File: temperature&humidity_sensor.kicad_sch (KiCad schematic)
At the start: 4 parts, among them U36 HDC1080

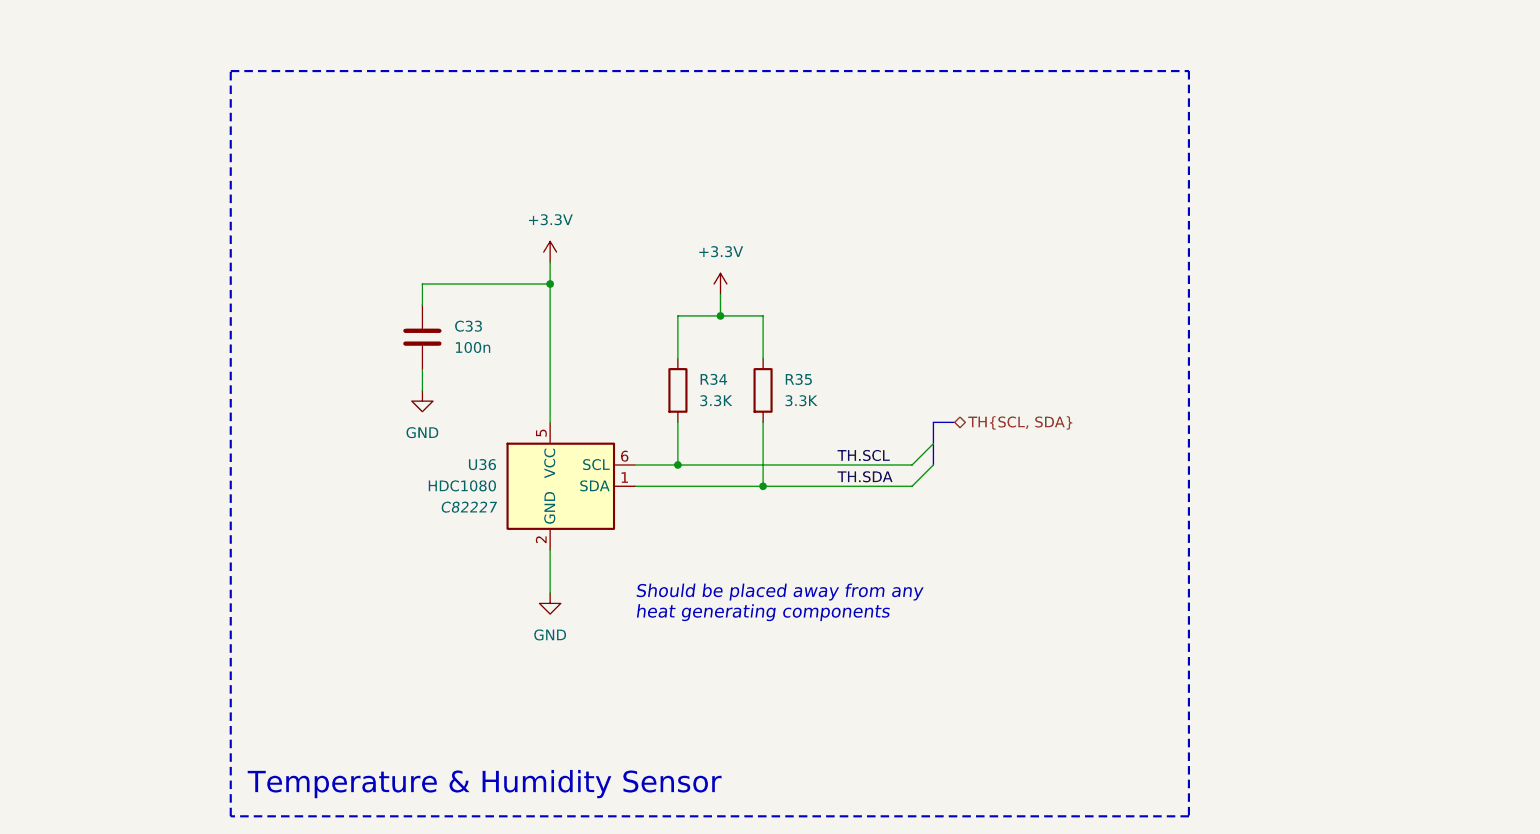
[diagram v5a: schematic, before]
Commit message: ESD, LEDs, footprints
- assignment of footprints
- ESD protection
- User buttons
- addition of test points
- BOM consolidation of  resistors
- general reordering of the schematic
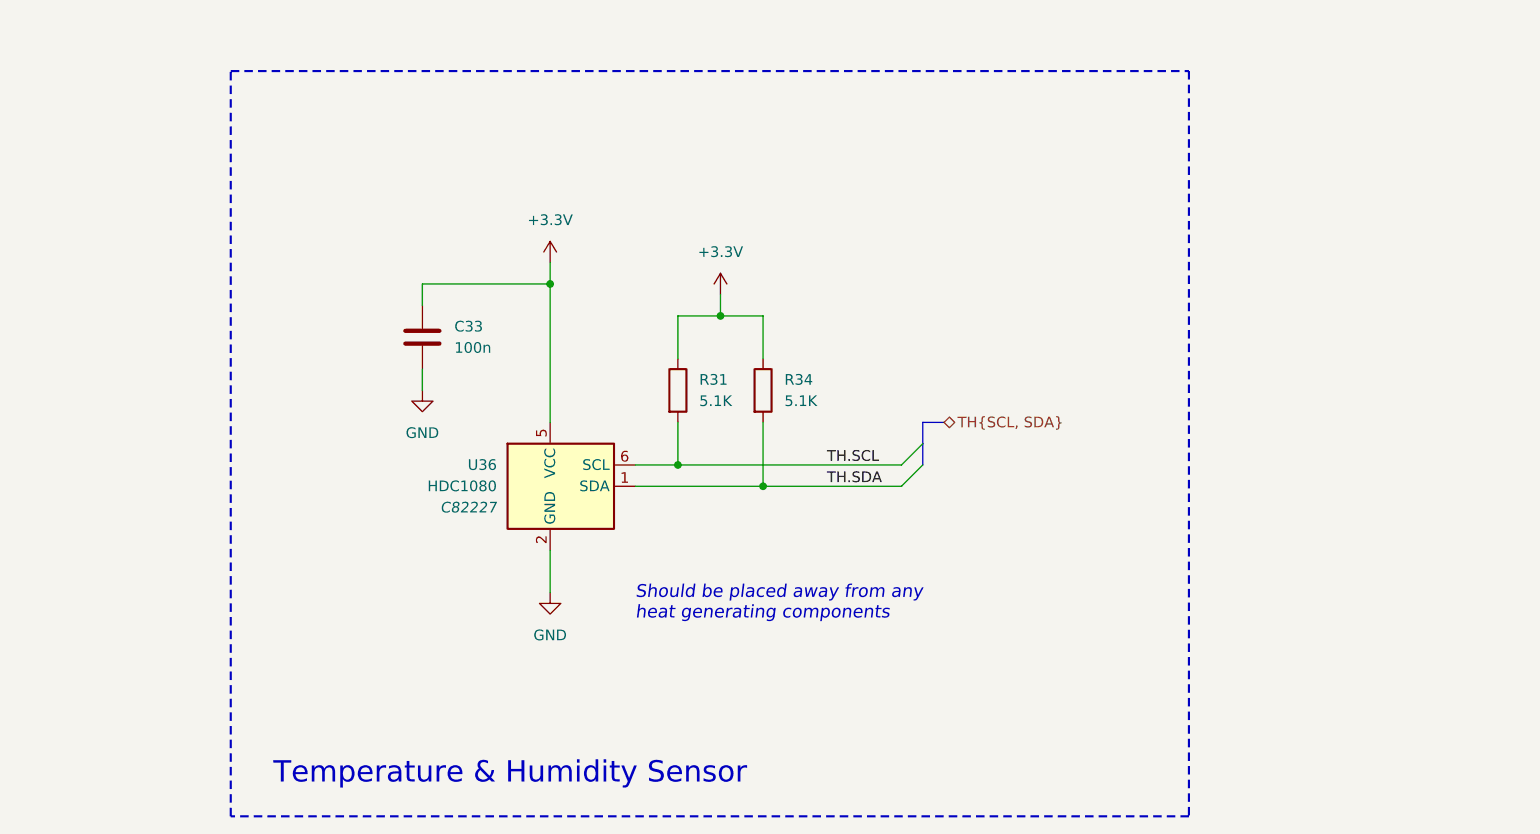
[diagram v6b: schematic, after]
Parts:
- removed R35: 3.3K, symbol Device:R
- added R31: 5.1K, Resistor_SMD:R_0603_1608Metric, symbol Device:R
- C33: footprint (none) -> Capacitor_SMD:C_0603_1608Metric
- R34: value 3.3K -> 5.1K; footprint (none) -> Resistor_SMD:R_0603_1608Metric
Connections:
- net +3.3V: now also R31.1
- net TH.SCL: now also R31.2; no longer R34.2
- net TH.SDA: now also R34.2
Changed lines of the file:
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@@
 	(title_block
 		(title "Temperature & Humidity Sensor")
-		(date "2025-10-31")
+		(date "2025-11-04")
 		(rev "v0.0")
 		(company "Rajath Katker")
@@
 	(text "Temperature & Humidity Sensor"
 		(exclude_from_sim no)
-		(at 84.582 142.24 0)
+		(at 87.63 140.97 0)
 		(effects
 			(font
@@
 	)
 	(bus_entry
-		(at 166.37 101.6)
+		(at 165.1 101.6)
 		(size -2.54 2.54)
 		(stroke
@@
 	)
 	(bus_entry
-		(at 166.37 104.14)
+		(at 165.1 104.14)
 		(size -2.54 2.54)
 		(stroke
@@
 	(wire
 		(pts
-			(xy 146.05 106.68) (xy 163.83 106.68)
+			(xy 146.05 106.68) (xy 162.56 106.68)
 		)
 		(stroke
@@
 	(wire
 		(pts
-			(xy 135.89 104.14) (xy 163.83 104.14)
+			(xy 135.89 104.14) (xy 162.56 104.14)
 		)
 		(stroke
@@
 	(bus
 		(pts
-			(xy 166.37 99.06) (xy 166.37 101.6)
+			(xy 165.1 99.06) (xy 165.1 101.6)
 		)
 		(stroke
@@
 	(bus
 		(pts
-			(xy 166.37 101.6) (xy 166.37 104.14)
+			(xy 165.1 101.6) (xy 165.1 104.14)
 		)
 		(stroke
@@
 	(bus
 		(pts
-			(xy 166.37 99.06) (xy 168.91 99.06)
+			(xy 165.1 99.06) (xy 167.64 99.06)
 		)
 		(stroke
@@
 	)
 	(label "TH.SCL"
-		(at 154.94 104.14 0)
+		(at 153.67 104.14 0)
 		(effects
 			(font
@@
 	)
 	(label "TH.SDA"
-		(at 154.94 106.68 0)
+		(at 153.67 106.68 0)
 		(effects
 			(font
@@
 	(hierarchical_label "TH{SCL, SDA}"
 		(shape bidirectional)
-		(at 168.91 99.06 0)
+		(at 167.64 99.06 0)
 		(effects
 			(font
@@
 	)
 	(symbol
-		(lib_id "Device:R")
-		(at 146.05 95.25 0)
-		(unit 1)
-		(exclude_from_sim no)
-		(in_bom yes)
-		(on_board yes)
-		(dnp no)
-		(fields_autoplaced yes)
-		(property "Reference" "R35"
-			(at 148.59 93.9799 0)
-			(effects
-				(font
-					(size 1.27 1.27)
-				)
-				(justify left)
-			)
-		)
-		(property "Value" "3.3K"
-			(at 148.59 96.5199 0)
-			(effects
-				(font
-					(size 1.27 1.27)
-				)
-				(justify left)
-			)
-		)
-		(property "Footprint" ""
-			(at 144.272 95.25 90)
-			(effects
-				(font
-					(size 1.27 1.27)
-				)
-				(hide yes)
-			)
-		)
-		(property "Datasheet" "~"
-			(at 146.05 95.25 0)
-			(effects
-				(font
-					(size 1.27 1.27)
-				)
-				(hide yes)
-			)
-		)
-		(property "Description" "Resistor"
-			(at 146.05 95.25 0)
-			(effects
-				(font
-					(size 1.27 1.27)
-				)
-				(hide yes)
-			)
-		)
-		(pin "2"
-		)
-		(pin "1"
-		)
-		(instances
-			(project "Precision Clock"
-				(path "/c9a8ff63-a0d1-4125-9dd1-40fb53daf536/cc882cab-fb20-4552-b867-43569dfc2d06"
-					(reference "R35")
-					(unit 1)
-				)
-			)
-		)
-	)
-	(symbol
 		(lib_id "power:+3.3V")
 		(at 140.97 83.82 0)
@@
 			)
 		)
-		(property "Footprint" ""
+		(property "Footprint" "Capacitor_SMD:C_0603_1608Metric"
 			(at 106.3752 92.71 0)
 			(effects
@@
 	)
 	(symbol
+		(lib_id "Sensor_Humidity:HDC1080")
+		(at 123.19 106.68 0)
+		(unit 1)
+		(exclude_from_sim no)
+		(in_bom yes)
+		(on_board yes)
+		(dnp no)
+		(property "Reference" "U36"
+			(at 114.3 104.14 0)
+			(effects
+				(font
+					(size 1.27 1.27)
+				)
+				(justify right)
+			)
+		)
+		(property "Value" "HDC1080"
+			(at 114.3 106.68 0)
+			(effects
+				(font
+					(size 1.27 1.27)
+				)
+				(justify right)
+			)
+		)
+		(property "Footprint" "Package_SON:Texas_PWSON-N6"
+			(at 121.92 113.03 0)
+			(effects
+				(font
+					(size 1.27 1.27)
+				)
+				(justify left)
+				(hide yes)
+			)
+		)
+		(property "Datasheet" "http://www.ti.com/lit/ds/symlink/hdc1080.pdf"
+			(at 113.03 100.33 0)
+			(effects
+				(font
+					(size 1.27 1.27)
+				)
+				(hide yes)
+			)
+		)
+		(property "Description" "Low Power,High Accuracy Digital Humidity Sensor with Temperature Sensor"
+			(at 123.19 106.68 0)
+			(effects
+				(font
+					(size 1.27 1.27)
+				)
+				(hide yes)
+			)
+		)
+		(property "LCSC" "C82227"
+			(at 114.3 109.2201 0)
+			(effects
+				(font
+					(size 1.27 1.27)
+					(italic yes)
+				)
+				(justify right)
+			)
+		)
+		(pin "7"
+		)
+		(pin "3"
+		)
+		(pin "5"
+		)
+		(pin "2"
+		)
+		(pin "4"
+		)
+		(pin "1"
+		)
+		(pin "6"
+		)
+		(instances
+			(project "Precision Clock"
+				(path "/c9a8ff63-a0d1-4125-9dd1-40fb53daf536/cc882cab-fb20-4552-b867-43569dfc2d06"
+					(reference "U36")
+					(unit 1)
+				)
+			)
+		)
+	)
+	(symbol
 		(lib_id "Device:R")
-		(at 135.89 95.25 0)
+		(at 146.05 95.25 0)
 		(unit 1)
 		(exclude_from_sim no)
@@
 		(fields_autoplaced yes)
 		(property "Reference" "R34"
-			(at 138.43 93.9799 0)
+			(at 148.59 93.9799 0)
 			(effects
 				(font
@@
 			)
 		)
-		(property "Value" "3.3K"
-			(at 138.43 96.5199 0)
+		(property "Value" "5.1K"
+			(at 148.59 96.5199 0)
 			(effects
 				(font
@@
 			)
 		)
-		(property "Footprint" ""
-			(at 134.112 95.25 90)
+		(property "Footprint" "Resistor_SMD:R_0603_1608Metric"
+			(at 144.272 95.25 90)
 			(effects
 				(font
@@
 		)
 		(property "Datasheet" "~"
-			(at 135.89 95.25 0)
+			(at 146.05 95.25 0)
 			(effects
 				(font
@@
 		)
 		(property "Description" "Resistor"
-			(at 135.89 95.25 0)
-			(effects
-				(font
-					(size 1.27 1.27)
-				)
-				(hide yes)
-			)
+			(at 146.05 95.25 0)
+			(effects
+				(font
+					(size 1.27 1.27)
+				)
+				(hide yes)
+			)
+		)
+		(pin "1"
 		)
 		(pin "2"
-		)
-		(pin "1"
 		)
 		(instances
@@
 				(path "/c9a8ff63-a0d1-4125-9dd1-40fb53daf536/cc882cab-fb20-4552-b867-43569dfc2d06"
 					(reference "R34")
-					(unit 1)
-				)
-			)
-		)
-	)
-	(symbol
-		(lib_id "Sensor_Humidity:HDC1080")
-		(at 123.19 106.68 0)
-		(unit 1)
-		(exclude_from_sim no)
-		(in_bom yes)
-		(on_board yes)
-		(dnp no)
-		(property "Reference" "U36"
-			(at 114.3 104.14 0)
-			(effects
-				(font
-					(size 1.27 1.27)
-				)
-				(justify right)
-			)
-		)
-		(property "Value" "HDC1080"
-			(at 114.3 106.68 0)
-			(effects
-				(font
-					(size 1.27 1.27)
-				)
-				(justify right)
-			)
-		)
-		(property "Footprint" "Package_SON:Texas_PWSON-N6"
-			(at 121.92 113.03 0)
-			(effects
-				(font
-					(size 1.27 1.27)
-				)
-				(justify left)
-				(hide yes)
-			)
-		)
-		(property "Datasheet" "http://www.ti.com/lit/ds/symlink/hdc1080.pdf"
-			(at 113.03 100.33 0)
-			(effects
-				(font
-					(size 1.27 1.27)
-				)
-				(hide yes)
-			)
-		)
-		(property "Description" "Low Power,High Accuracy Digital Humidity Sensor with Temperature Sensor"
-			(at 123.19 106.68 0)
-			(effects
-				(font
-					(size 1.27 1.27)
-				)
-				(hide yes)
-			)
-		)
-		(property "LCSC" "C82227"
-			(at 114.3 109.2201 0)
-			(effects
-				(font
-					(size 1.27 1.27)
-					(italic yes)
-				)
-				(justify right)
-			)
-		)
-		(pin "7"
-		)
-		(pin "3"
-		)
-		(pin "5"
-		)
-		(pin "2"
-		)
-		(pin "4"
-		)
-		(pin "1"
-		)
-		(pin "6"
-		)
-		(instances
-			(project "Precision Clock"
-				(path "/c9a8ff63-a0d1-4125-9dd1-40fb53daf536/cc882cab-fb20-4552-b867-43569dfc2d06"
-					(reference "U36")
 					(unit 1)
 				)
@@
 					(unit 1)
 				)
+			)
+		)
+	)
+	(symbol
+		(lib_id "Device:R")
+		(at 135.89 95.25 0)
+		(unit 1)
+		(exclude_from_sim no)
+		(in_bom yes)
+		(on_board yes)
+		(dnp no)
+		(fields_autoplaced yes)
+		(property "Reference" "R31"
+			(at 138.43 93.9799 0)
+			(effects
+				(font
+					(size 1.27 1.27)
+				)
+				(justify left)
+			)
+		)
+		(property "Value" "5.1K"
+			(at 138.43 96.5199 0)
+			(effects
+				(font
+					(size 1.27 1.27)
+				)
+				(justify left)
+			)
+		)
+		(property "Footprint" "Resistor_SMD:R_0603_1608Metric"
+			(at 134.112 95.25 90)
+			(effects
+				(font
+					(size 1.27 1.27)
+				)
+				(hide yes)
+			)
+		)
+		(property "Datasheet" "~"
+			(at 135.89 95.25 0)
+			(effects
+				(font
+					(size 1.27 1.27)
+				)
+				(hide yes)
+			)
+		)
+		(property "Description" "Resistor"
+			(at 135.89 95.25 0)
+			(effects
+				(font
+					(size 1.27 1.27)
+				)
+				(hide yes)
+			)
+		)
+		(pin "1"
+		)
+		(pin "2"
+		)
+		(instances
+			(project "Precision Clock"
+				(path "/c9a8ff63-a0d1-4125-9dd1-40fb53daf536/cc882cab-fb20-4552-b867-43569dfc2d06"
+					(reference "R31")
+					(unit 1)
+				)

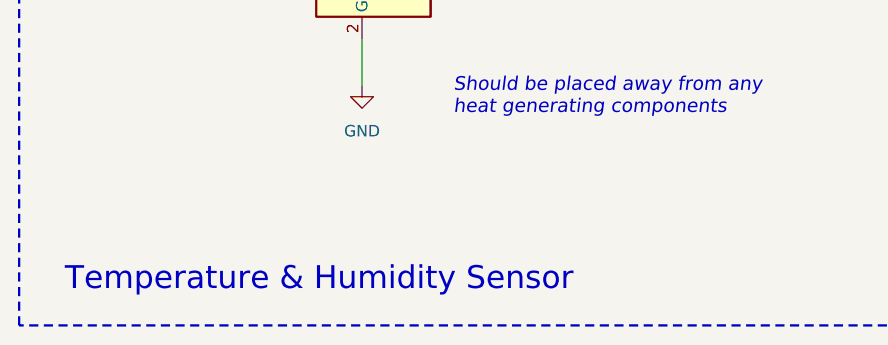
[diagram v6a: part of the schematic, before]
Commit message: verification
- sensor schematic verification
- change in the value of current limiting resistor
- disconnected unused buffer pins
- labeling or peripherals used in primary MCU
- additional user button
- DRC corrections
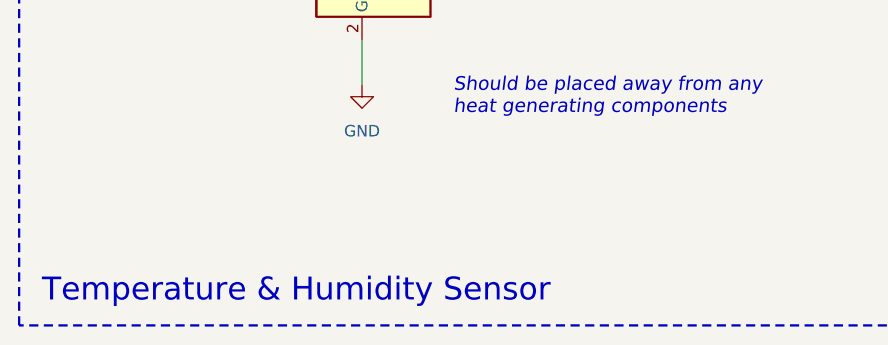
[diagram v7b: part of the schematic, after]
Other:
- company: Rajath Katker -> TJ71PL
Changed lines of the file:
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@@
 	(title_block
 		(title "Temperature & Humidity Sensor")
-		(date "2025-11-04")
+		(date "2025-09-05")
 		(rev "v0.0")
-		(company "Rajath Katker")
-		(comment 4 "Final verification pending")
+		(company "TJ71PL")
+		(comment 1 "天計")
+		(comment 4 "Final verification complete")
 	)
 	(rectangle
@@
 	(text "Temperature & Humidity Sensor"
 		(exclude_from_sim no)
-		(at 87.63 140.97 0)
+		(at 85.09 142.24 0)
 		(effects
 			(font
@@
 		)
 	)
+	(table
+		(column_count 2)
+		(border
+			(external yes)
+			(header yes)
+			(stroke
+				(width 0.2032)
+				(type solid)
+				(color 132 0 0 1)
+			)
+		)
+		(separators
+			(rows yes)
+			(cols yes)
+			(stroke
+				(width 0.2032)
+				(type solid)
+				(color 132 0 0 1)
+			)
+		)
+		(column_widths 17.78 12.7)
+		(row_heights 3.81 3.81 3.81 3.81)
+		(cells
+			(table_cell "Iload (max)"
+				(exclude_from_sim no)
+				(at 163.83 128.27 0)
+				(size 17.78 3.81)
+				(margins 0.9525 0.9525 0.9525 0.9525)
+				(span 1 1)
+				(fill
+					(type none)
+				)
+				(effects
+					(font
+						(size 1.27 1.27)
+						(color 132 0 0 1)
+					)
+				)
+			)
+			(table_cell "1.3uA"
+				(exclude_from_sim no)
+				(at 181.61 128.27 0)
+				(size 12.7 3.81)
+				(margins 0.9525 0.9525 0.9525 0.9525)
+				(span 1 1)
+				(fill
+					(type none)
+				)
+				(effects
+					(font
+						(size 1.27 1.27)
+						(color 132 0 0 1)
+					)
+				)
+			)
+			(table_cell "Istartup"
+				(exclude_from_sim no)
+				(at 163.83 132.08 0)
+				(size 17.78 3.81)
+				(margins 0.9525 0.9525 0.9525 0.9525)
+				(span 1 1)
+				(fill
+					(type none)
+				)
+				(effects
+					(font
+						(size 1.27 1.27)
+						(color 132 0 0 1)
+					)
+				)
+			)
+			(table_cell "300uA"
+				(exclude_from_sim no)
+				(at 181.61 132.08 0)
+				(size 12.7 3.81)
+				(margins 0.9525 0.9525 0.9525 0.9525)
+				(span 1 1)
+				(fill
+					(type none)
+				)
+				(effects
+					(font
+						(size 1.27 1.27)
+						(color 132 0 0 1)
+					)
+				)
+			)
+			(table_cell "Iheater"
+				(exclude_from_sim no)
+				(at 163.83 135.89 0)
+				(size 17.78 3.81)
+				(margins 0.9525 0.9525 0.9525 0.9525)
+				(span 1 1)
+				(fill
+					(type none)
+				)
+				(effects
+					(font
+						(size 1.27 1.27)
+						(color 132 0 0 1)
+					)
+				)
+			)
+			(table_cell "7.2mA"
+				(exclude_from_sim no)
+				(at 181.61 135.89 0)
+				(size 12.7 3.81)
+				(margins 0.9525 0.9525 0.9525 0.9525)
+				(span 1 1)
+				(fill
+					(type none)
+				)
+				(effects
+					(font
+						(size 1.27 1.27)
+						(color 132 0 0 1)
+					)
+				)
+			)
+			(table_cell "P (max)"
+				(exclude_from_sim no)
+				(at 163.83 139.7 0)
+				(size 17.78 3.81)
+				(margins 0.9525 0.9525 0.9525 0.9525)
+				(span 1 1)
+				(fill
+					(type none)
+				)
+				(effects
+					(font
+						(size 1.27 1.27)
+						(color 132 0 0 1)
+					)
+				)
+			)
+			(table_cell "25mW"
+				(exclude_from_sim no)
+				(at 181.61 139.7 0)
+				(size 12.7 3.81)
+				(margins 0.9525 0.9525 0.9525 0.9525)
+				(span 1 1)
+				(fill
+					(type none)
+				)
+				(effects
+					(font
+						(size 1.27 1.27)
+						(color 132 0 0 1)
+					)
+				)
+			)
+		)
+	)
